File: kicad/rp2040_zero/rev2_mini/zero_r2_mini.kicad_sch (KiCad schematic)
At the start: 3 parts, among them J3 Debug port, J5 Debug port, U1 RP2040-Zero

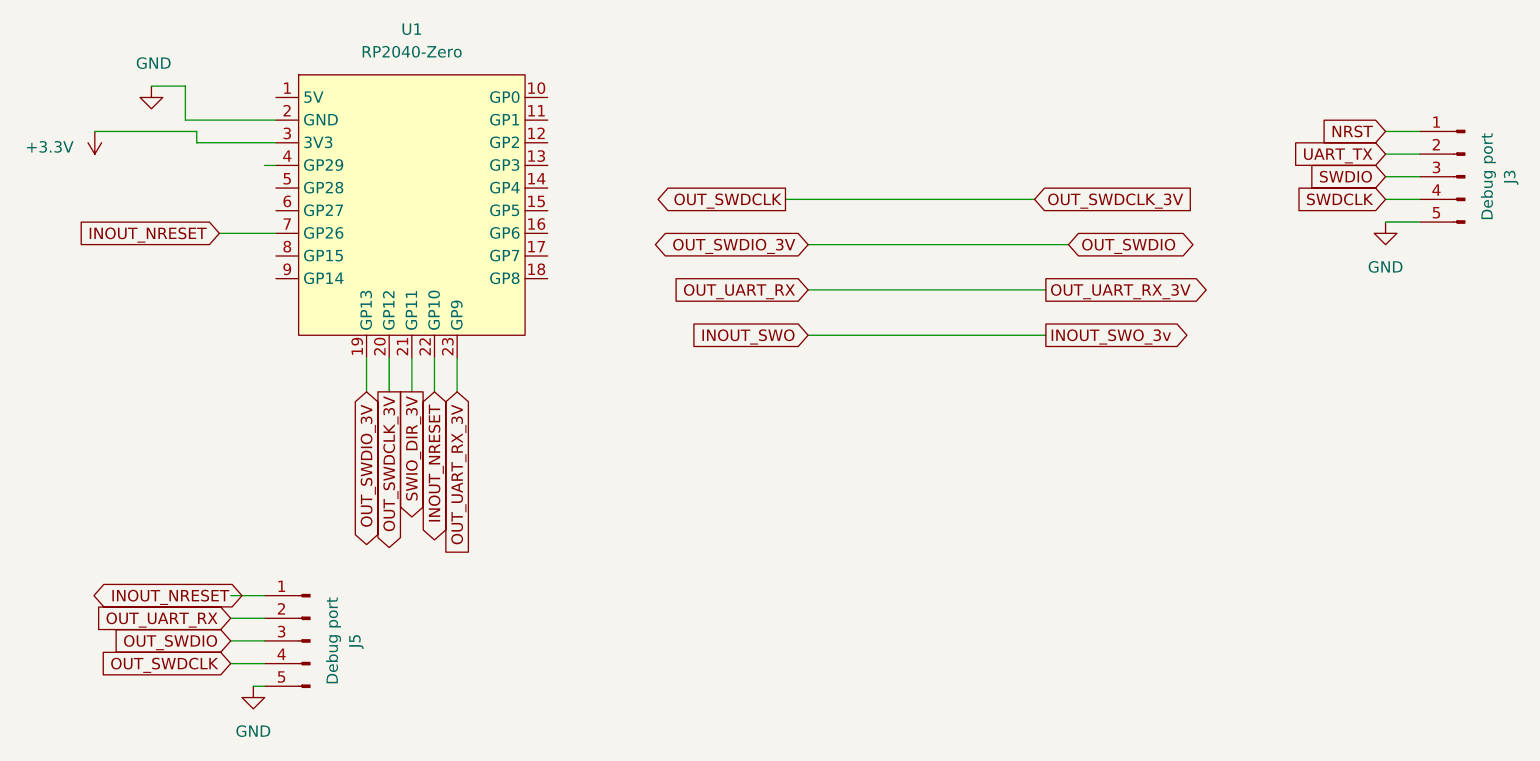
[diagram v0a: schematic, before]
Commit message: kicad: RP mini , add reset mosfet
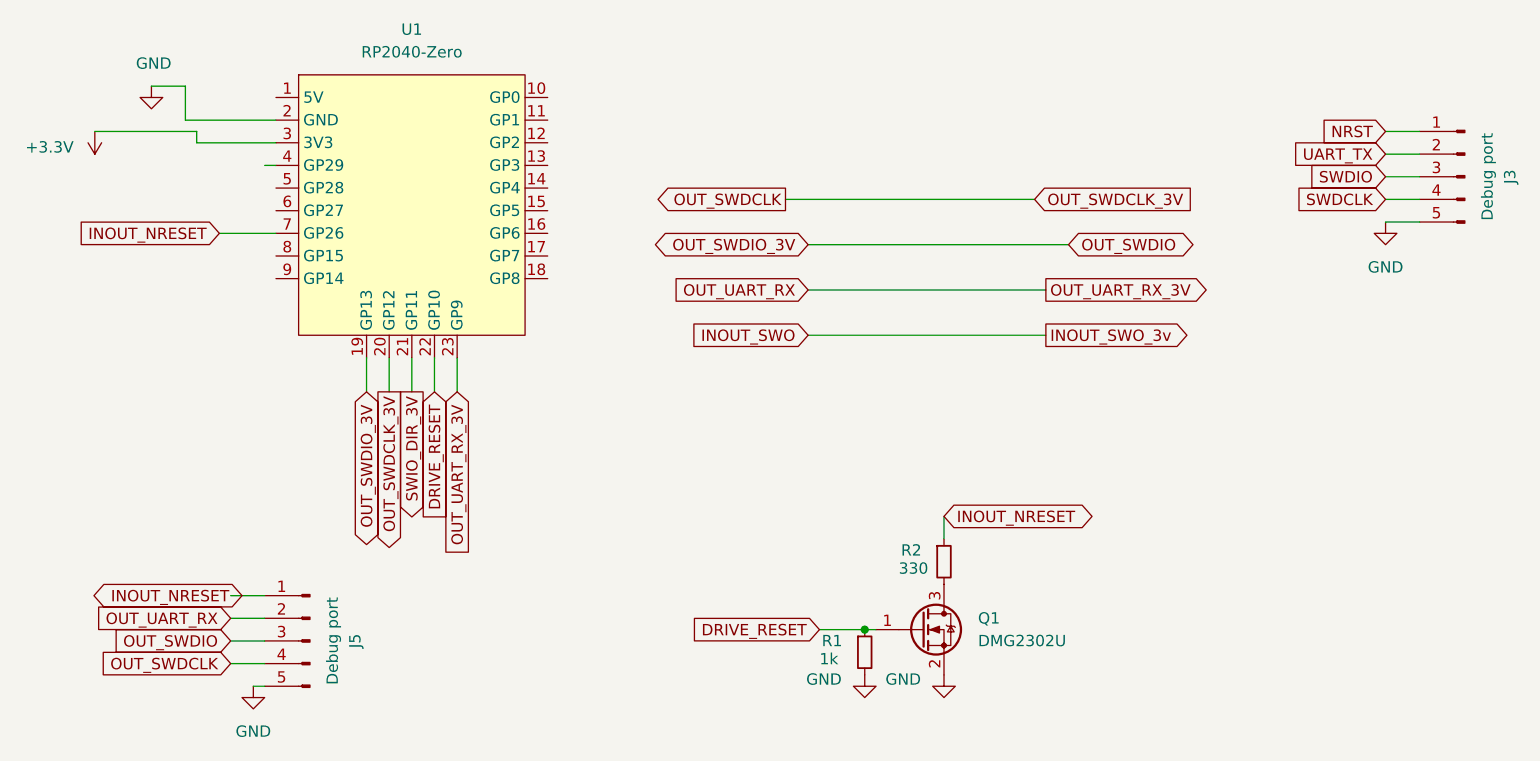
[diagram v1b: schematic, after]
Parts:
- added Q1: DMG2302U, Package_TO_SOT_SMD:SOT-23, symbol Transistor_FET:DMG2302U
- added R1: 1k, Resistor_SMD:R_0603_1608Metric, symbol Device:R_Small
- added R2: 330, Resistor_SMD:R_0603_1608Metric, symbol Device:R_Small
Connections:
- net GND: now also Q1.2 (S), R1.2
- net INOUT_NRESET: now also R2.1; no longer U1.22 (GP10)
- new net: Q1.3 (D), R2.2
- new net DRIVE_RESET: Q1.1 (G), R1.1, U1.22 (GP10)
